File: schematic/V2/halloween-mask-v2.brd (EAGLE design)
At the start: 97 x 32 mm, 22 parts, among them J1 EL-Wire-Inverter, J5 PIR, Q1 IRLB8721PBF, U1 MCP1826T-3302E_DC, U2 Adafruit-ITSY-BITSY-M0

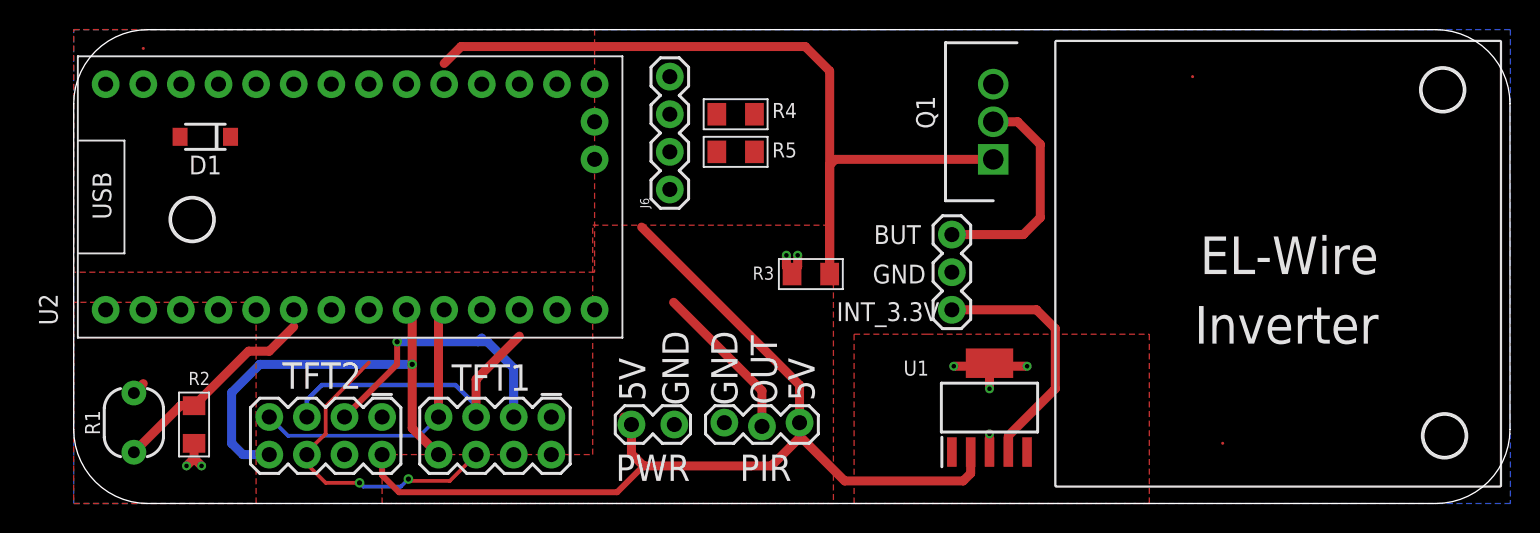
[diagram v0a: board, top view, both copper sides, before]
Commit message: Added a connector for ToF. Added a schotky diode from Vusb to Vbat, so that I can both use external power and USB.
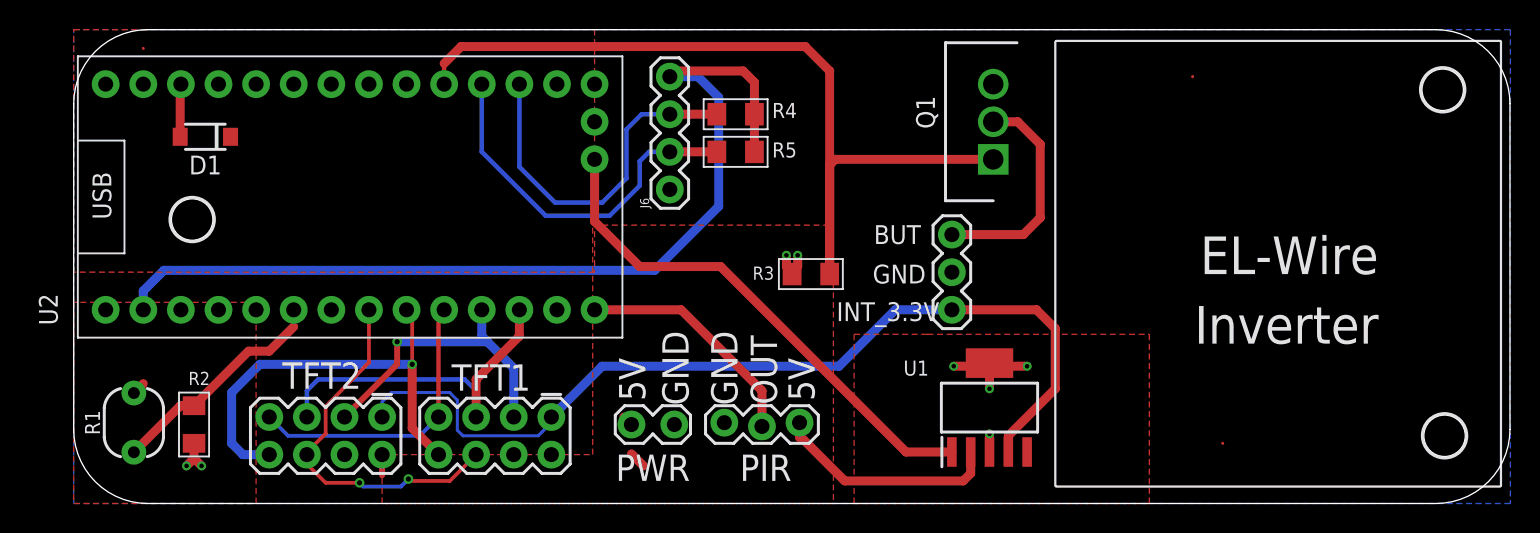
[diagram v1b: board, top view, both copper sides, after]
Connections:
- removed net N$9: R4.2, R5.2
- net 3.3V: now also R4.2, R5.2
- net SCL: now also J6.2, R5.1; no longer J6.3, R4.1
- net SDA: now also J6.3, R4.1; no longer J6.2, R5.1
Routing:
- net 3.3V: track 0.90 -> 65.5 mm
- net 5V: track 69.4 -> 19.6 mm
- net BACKLIGHT_3.3V: track 17.2 -> 63.1 mm
- net D3: track 0.00 -> 34.8 mm
- net SCL: track 0.00 -> 25.0 mm
- net SDA: track 0.00 -> 24.3 mm
- net PIR_OUT: track 10.9 -> 16.0 mm
- net N$1: track 0.00 -> 3.58 mm
- net CS: track 21.7 -> 25.2 mm
- net MOSI: track 21.0 -> 24.1 mm
- net SCK: track 18.8 -> 20.8 mm
- net N$3: track 59.5 -> 60.9 mm
- net LDR_A1: track 14.3 -> 15.4 mm
